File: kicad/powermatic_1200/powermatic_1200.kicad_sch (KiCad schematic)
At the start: 26 parts, among them J1 T4171310004-001, J2 3PH-4W-PLUG, K1 HMC-9B30-11-DS, K2 HMC-9B30-11-DS, K3 HC3096N-52-900-24, K4 HMC-9B30-11-DS, K5 HMC-9B30-11-DS, K6 HMC-9B30-11-DS, M1 PWRM1200-MOTOR, Q1 FAZ-D4/2-NA-L, SW1 222102

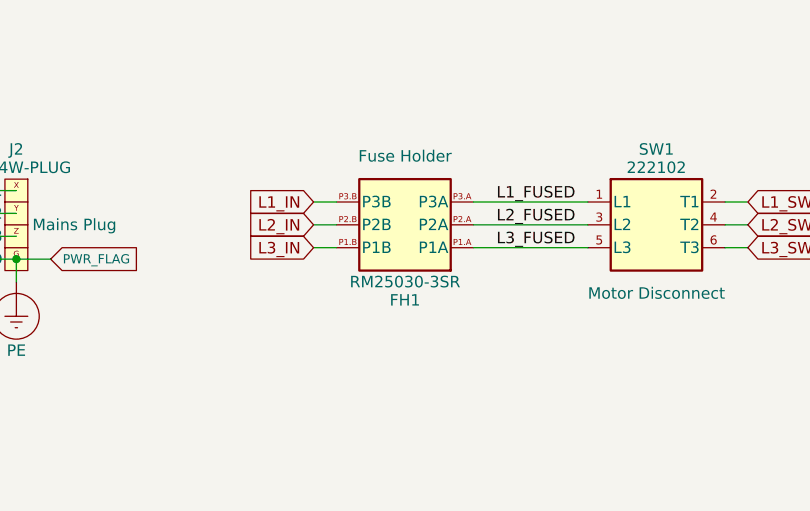
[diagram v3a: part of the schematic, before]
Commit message: Configure DIN routing grids and update fuse-holder layout
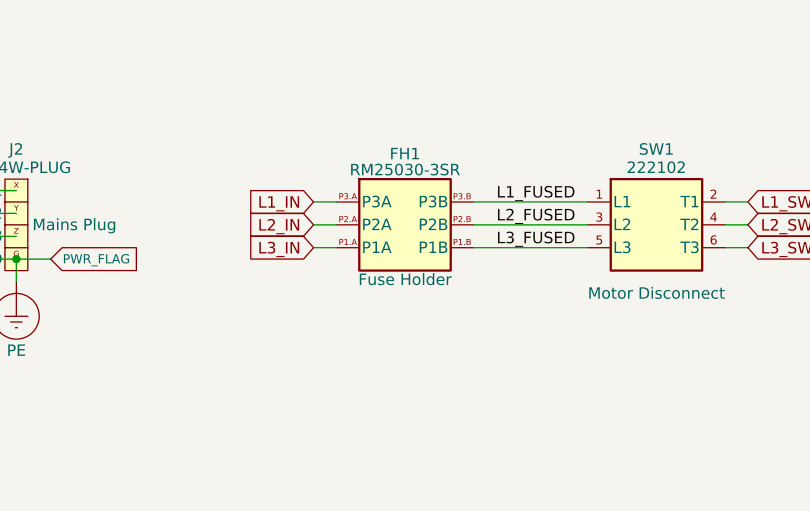
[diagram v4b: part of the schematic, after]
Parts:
- removed FH1: RM25030-3SR, Controls:RM25030-3SR_Front, symbol non_lcsc_parts:Non-LCSC/RM25030-3SR
- added FH1: RM25030-3SR, Controls:RM25030-3SR_Front, symbol Controls:RM25030-3SR
- K1, K2, K4, K5, K6: footprint Controls:HMC-9B30-11-DS_Front -> Controls:HMC-9B30-11-DS_Front_Grid1mm
- K3: footprint Controls:HC3096N-52-900-24_Front -> Controls:HC3096N-52-900-24_Front_Grid1mm
- OL4, OL6: footprint Controls:HTOR32-6-S_Front -> Controls:HTOR32-6-S_Front_Grid1mm
- PS1: footprint Controls:NDR-240-24_Front -> Controls:NDR-240-24_Front_Grid1mm
- Q1: footprint Controls:FAZ-D4-2-NA-L_Front -> Controls:FAZ-D4-2-NA-L_Front_Grid1mm
- SP1, SP2, SP4, SP5, SP6: footprint Controls:HMX1-SSVRC-DC_Front -> Controls:HMX1-SSVRC-DC_Front_Grid1mm
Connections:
- net L1_FUSED: now also FH1.P3.B (P3B)
- net L1_IN: now also FH1.P3.A (P3A)
- net L2_FUSED: now also FH1.P2.B (P2B)
- net L2_IN: now also FH1.P2.A (P2A)
- net L3_FUSED: now also FH1.P1.B (P1B)
- net L3_IN: now also FH1.P1.A (P1A)

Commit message: updated S2, S3, and M1
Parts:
- M1: footprint (none) -> Controls:PWRM1200-MOTOR_Top_150mm; Package (none) -> Machine motor (150 mm illustrative top view)
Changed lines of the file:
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@@
 		(exclude_from_sim no)
 		(in_bom yes)
-		(on_board no)
-		(in_pos_files yes)
+		(on_board yes)
+		(in_pos_files no)
 		(dnp no)
 		(property "Reference" "M1"
@@
 			)
 		)
-		(property "Footprint" ""
+		(property "Footprint" "Controls:PWRM1200-MOTOR_Top_150mm"
 			(at 302.26 -7.62 0)
 			(hide yes)
@@
 			)
 		)
-		(property "Package" ""
+		(property "Package" "Machine motor (150 mm illustrative top view)"
 			(at 302.26 -7.62 0)
 			(hide yes)

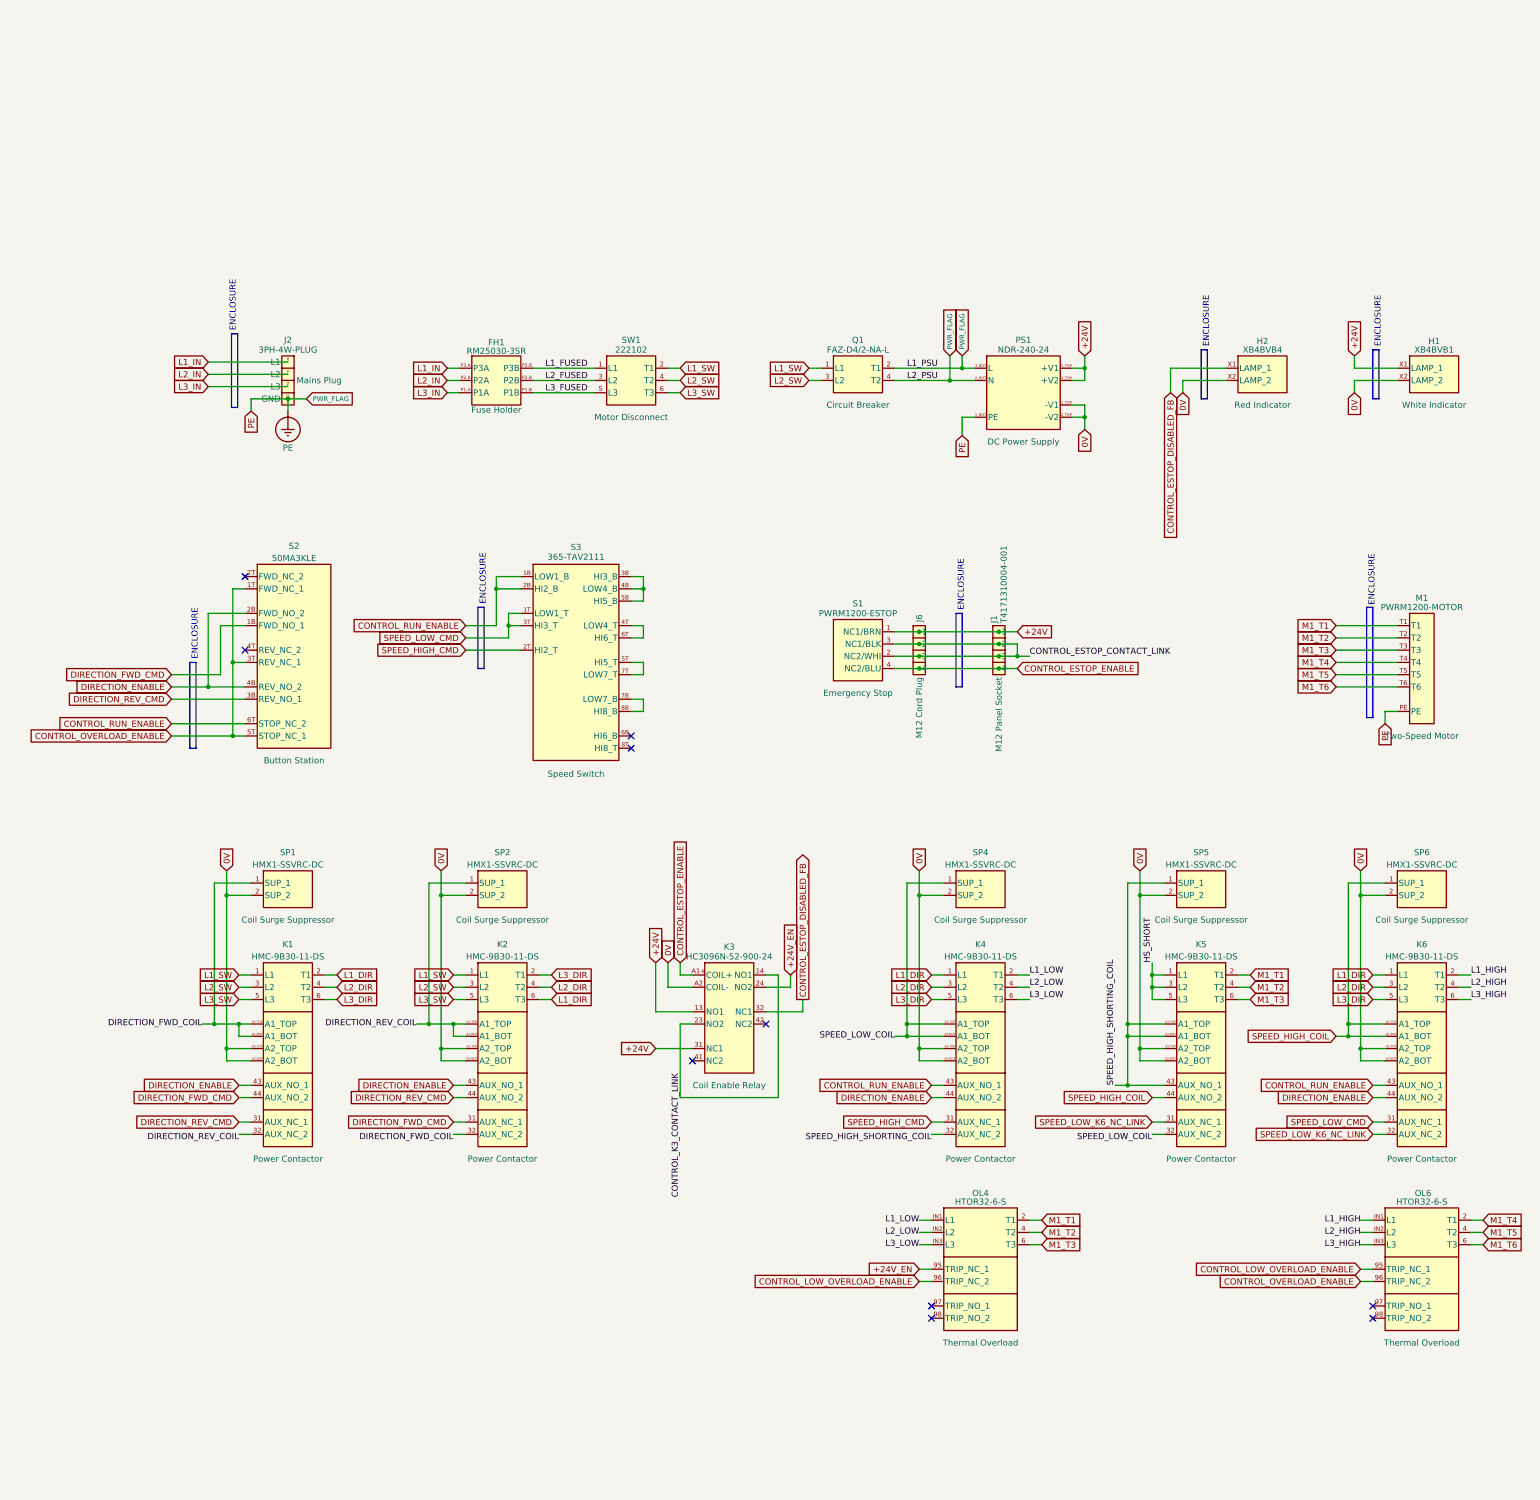
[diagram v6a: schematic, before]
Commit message: Update saved control schematic and panel layout
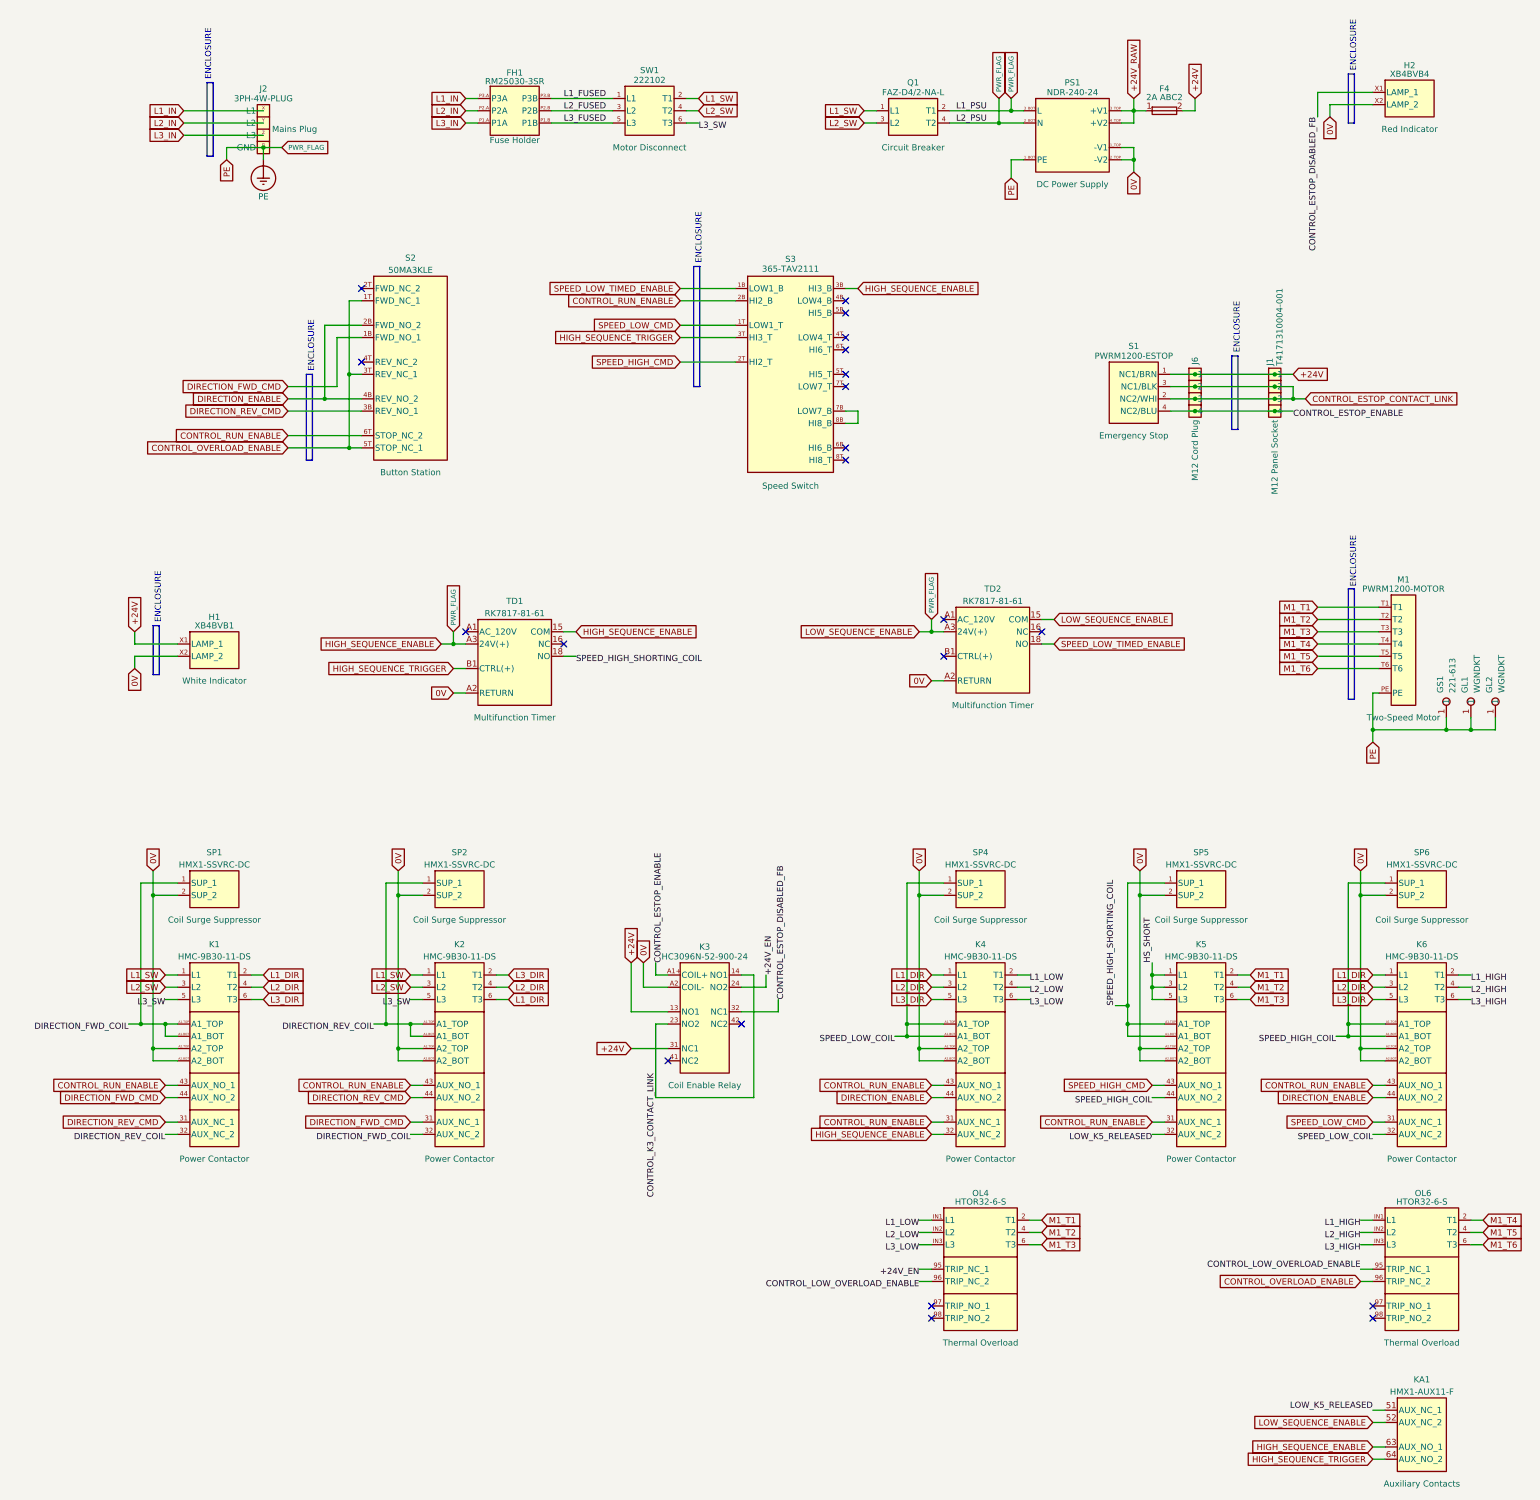
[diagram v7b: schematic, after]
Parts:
- added F4: 2A ABC2, Controls:281-623_Front, symbol Generics:Fuse
- added GL1, GL2: WGNDKT, LCSC:TestPoint_Pad_D3.0mm, symbol Generics:TestPoint
- added GS1: 221-613, LCSC:TestPoint_Pad_D3.0mm, symbol Generics:TestPoint
- added KA1: HMX1-AUX11-F, Controls:HMX1-AUX11-F_Front, symbol Controls:HMX1-AUX11-F
- added TD1, TD2: RK7817-81-61, Controls:RK7817-81-61_Front, symbol Controls:RK7817-81-61
- J1: Wire.Sizes {"schema":1,"owner_uuid":"b4d1b4ae-f9ca-4a9a-a340-a64e26a697f9","entries":[{"pin":"1","net":"+24V","scope":"factory_pigtail","awg":22,"color":"Brown","note":"T4171310004-001 factory 0.34 mm² / 22 AWG lead; any extension is a separate wire."},{"pin":"2","net":"/CONTROL_ESTOP_CONTACT_LINK","scope":"factory_pigtail","awg":22,"color":"White","note":"T4171310004-001 factory 0.34 mm² / 22 AWG lead; any extension is a separate wire."},{"pin":"3","net":"/CONTROL_ESTOP_CONTACT_LINK","scope":"factory_pigtail","awg":22,"color":"Blue","note":"T4171310004-001 factory 0.34 mm² / 22 AWG lead; any extension is a separate wire."},{"pin":"4","net":"CONTROL_ESTOP_ENABLE","scope":"factory_pigtail","awg":22,"color":"Black","note":"T4171310004-001 factory 0.34 mm² / 22 AWG lead; any extension is a separate wire."}]} -> {"schema":1,"owner_uuid":"b4d1b4ae-f9ca-4a9a-a340-a64e26a697f9","entries":[{"pin":"1","net":"+24V","scope":"factory_pigtail","awg":22,"color":"Brown","note":"T4171310004-001 factory 0.34 mm\u00b2 / 22 AWG lead; any extension is a separate wire."},{"pin":"2","net":"CONTROL_ESTOP_CONTACT_LINK","scope":"factory_pigtail","awg":22,"color":"White","note":"T4171310004-001 factory 0.34 mm\u00b2 / 22 AWG lead; any extension is a separate wire."},{"pin":"3","net":"CONTROL_ESTOP_CONTACT_LINK","scope":"factory_pigtail","awg":22,"color":"Blue","note":"T4171310004-001 factory 0.34 mm\u00b2 / 22 AWG lead; any extension is a separate wire."},{"pin":"4","net":"/CONTROL_ESTOP_ENABLE","scope":"factory_pigtail","awg":22,"color":"Black","note":"T4171310004-001 factory 0.34 mm\u00b2 / 22 AWG lead; any extension is a separate wire."}]}
- J6: Wire.Sizes {"schema":1,"owner_uuid":"b5200e46-0e22-4b8b-8db6-9eae3d708854","entries":[{"pin":"1","net":"+24V","scope":"connector_interface","awg":null,"note":"M12 mating interface; retain the supplied assembly."},{"pin":"2","net":"/CONTROL_ESTOP_CONTACT_LINK","scope":"connector_interface","awg":null,"note":"M12 mating interface; retain the supplied assembly."},{"pin":"3","net":"/CONTROL_ESTOP_CONTACT_LINK","scope":"connector_interface","awg":null,"note":"M12 mating interface; retain the supplied assembly."},{"pin":"4","net":"CONTROL_ESTOP_ENABLE","scope":"connector_interface","awg":null,"note":"M12 mating interface; retain the supplied assembly."}]} -> {"schema":1,"owner_uuid":"b5200e46-0e22-4b8b-8db6-9eae3d708854","entries":[{"pin":"1","net":"+24V","scope":"connector_interface","awg":null,"note":"M12 mating interface; retain the supplied assembly."},{"pin":"2","net":"CONTROL_ESTOP_CONTACT_LINK","scope":"connector_interface","awg":null,"note":"M12 mating interface; retain the supplied assembly."},{"pin":"3","net":"CONTROL_ESTOP_CONTACT_LINK","scope":"connector_interface","awg":null,"note":"M12 mating interface; retain the supplied assembly."},{"pin":"4","net":"/CONTROL_ESTOP_ENABLE","scope":"connector_interface","awg":null,"note":"M12 mating interface; retain the supplied assembly."}]}
- K1: footprint Controls:HMC-9B30-11-DS_Front_Grid1mm -> Controls:HMC-9B30-11-DS_Front; Wire.Sizes {"schema":1,"owner_uuid":"d223283d-de9b-4327-854a-5af43f940011","entries":[{"pin":"1","net":"L1_SW","scope":"panel_power","awg":14,"color":"Black","note":"Gauge for discrete panel wire; reversing connection-kit bars retain their supplied form."},{"pin":"2","net":"L1_DIR","scope":"panel_power","awg":14,"color":"Black","note":"Gauge for discrete panel wire; reversing connection-kit bars retain their supplied form."},{"pin":"3","net":"L2_SW","scope":"panel_power","awg":14,"color":"Black","note":"Gauge for discrete panel wire; reversing connection-kit bars retain their supplied form."},{"pin":"31","net":"DIRECTION_REV_CMD","scope":"panel_control","awg":18,"color":"Blue"},{"pin":"32","net":"/DIRECTION_REV_COIL","scope":"panel_control","awg":18,"color":"Blue"},{"pin":"4","net":"L2_DIR","scope":"panel_power","awg":14,"color":"Black","note":"Gauge for discrete panel wire; reversing connection-kit bars retain their supplied form."},{"pin":"43","net":"DIRECTION_ENABLE","scope":"panel_control","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 -> {"schema":1,"owner_uuid":"d223283d-de9b-4327-854a-5af43f940011","entries":[{"pin":"1","net":"L1_SW","scope":"panel_power","awg":14,"color":"Black","note":"Gauge for discrete panel wire; reversing connection-kit bars retain their supplied form."},{"pin":"2","net":"L1_DIR","scope":"panel_power","awg":14,"color":"Black","note":"Gauge for discrete panel wire; reversing connection-kit bars retain their supplied form."},{"pin":"3","net":"L2_SW","scope":"panel_power","awg":14,"color":"Black","note":"Gauge for discrete panel wire; reversing connection-kit bars retain their supplied form."},{"pin":"31","net":"DIRECTION_REV_CMD","scope":"panel_control","awg":18,"color":"Blue"},{"pin":"32","net":"/DIRECTION_REV_COIL","scope":"panel_control","awg":18,"color":"Blue"},{"pin":"4","net":"L2_DIR","scope":"panel_power","awg":14,"color":"Black","note":"Gauge for discrete panel wire; reversing connection-kit bars retain their supplied form."},{"pin":"43","net":"CONTROL_RUN_ENABLE","scope":"panel_control"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
- K2: footprint Controls:HMC-9B30-11-DS_Front_Grid1mm -> Controls:HMC-9B30-11-DS_Front; Wire.Sizes {"schema":1,"owner_uuid":"e654422b-9a6f-4ebb-86fa-0867c299ae4a","entries":[{"pin":"1","net":"L1_SW","scope":"panel_power","awg":14,"color":"Black","note":"Gauge for discrete panel wire; reversing connection-kit bars retain their supplied form."},{"pin":"2","net":"L3_DIR","scope":"panel_power","awg":14,"color":"Black","note":"Gauge for discrete panel wire; reversing connection-kit bars retain their supplied form."},{"pin":"3","net":"L2_SW","scope":"panel_power","awg":14,"color":"Black","note":"Gauge for discrete panel wire; reversing connection-kit bars retain their supplied form."},{"pin":"31","net":"DIRECTION_FWD_CMD","scope":"panel_control","awg":18,"color":"Blue"},{"pin":"32","net":"/DIRECTION_FWD_COIL","scope":"panel_control","awg":18,"color":"Blue"},{"pin":"4","net":"L2_DIR","scope":"panel_power","awg":14,"color":"Black","note":"Gauge for discrete panel wire; reversing connection-kit bars retain their supplied form."},{"pin":"43","net":"DIRECTION_ENABLE","scope":"panel_control","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 -> {"schema":1,"owner_uuid":"e654422b-9a6f-4ebb-86fa-0867c299ae4a","entries":[{"pin":"1","net":"L1_SW","scope":"panel_power","awg":14,"color":"Black","note":"Gauge for discrete panel wire; reversing connection-kit bars retain their supplied form."},{"pin":"2","net":"L3_DIR","scope":"panel_power","awg":14,"color":"Black","note":"Gauge for discrete panel wire; reversing connection-kit bars retain their supplied form."},{"pin":"3","net":"L2_SW","scope":"panel_power","awg":14,"color":"Black","note":"Gauge for discrete panel wire; reversing connection-kit bars retain their supplied form."},{"pin":"31","net":"DIRECTION_FWD_CMD","scope":"panel_control","awg":18,"color":"Blue"},{"pin":"32","net":"/DIRECTION_FWD_COIL","scope":"panel_control","awg":18,"color":"Blue"},{"pin":"4","net":"L2_DIR","scope":"panel_power","awg":14,"color":"Black","note":"Gauge for discrete panel wire; reversing connection-kit bars retain their supplied form."},{"pin":"43","net":"CONTROL_RUN_ENABLE","scope":"panel_control"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
- K3: footprint Controls:HC3096N-52-900-24_Front_Grid1mm -> Controls:HC3096N-52-900-24_Front; Wire.Sizes {"schema":1,"owner_uuid":"40692fa1-1db0-4fd6-bab3-8a72882b147f","entries":[{"pin":"13","net":"+24V","scope":"panel_control","awg":18,"color":"Blue"},{"pin":"14","net":"/CONTROL_K3_CONTACT_LINK","scope":"panel_control","awg":18,"color":"Blue"},{"pin":"23","net":"/CONTROL_K3_CONTACT_LINK","scope":"panel_control","awg":18,"color":"Blue"},{"pin":"24","net":"+24V_EN","scope":"panel_control","awg":18,"color":"Blue"},{"pin":"A1+","net":"CONTROL_ESTOP_ENABLE","scope":"panel_control","awg":18,"color":"Blue"},{"pin":"A2","net":"0V","scope":"panel_control","awg":18,"color":"Blue"},{"pin":"31","net":"+24V","scope":"panel_control","awg":18,"color":"Blue"},{"pin":"32","net":"CONTROL_ESTOP_DISABLED_FB","scope":"panel_control","awg":18,"color":"Blue"}]} -> {"schema":1,"owner_uuid":"40692fa1-1db0-4fd6-bab3-8a72882b147f","entries":[{"pin":"13","net":"+24V","scope":"panel_control","awg":18,"color":"Blue"},{"pin":"14","net":"/CONTROL_K3_CONTACT_LINK","scope":"panel_control","awg":18,"color":"Blue"},{"pin":"23","net":"/CONTROL_K3_CONTACT_LINK","scope":"panel_control","awg":18,"color":"Blue"},{"pin":"24","net":"/+24V_EN","scope":"panel_control","awg":18,"color":"Blue"},{"pin":"A1+","net":"/CONTROL_ESTOP_ENABLE","scope":"panel_control","awg":18,"color":"Blue"},{"pin":"A2","net":"0V","scope":"panel_control","awg":18,"color":"Blue"},{"pin":"31","net":"+24V","scope":"panel_control","awg":18,"color":"Blue"},{"pin":"32","net":"/CONTROL_ESTOP_DISABLED_FB","scope":"panel_control","awg":18,"color":"Blue"}]}
- K4: footprint Controls:HMC-9B30-11-DS_Front_Grid1mm -> Controls:HMC-9B30-11-DS_Front; Wire.Sizes {"schema":1,"owner_uuid":"e783227f-ae21-4b33-9926-7527202601c5","entries":[{"pin":"1","net":"L1_DIR","scope":"panel_power","awg":14,"color":"Black","note":"Gauge for discrete panel wire; reversing connection-kit bars retain their supplied form."},{"pin":"2","net":"/L1_LOW","scope":"direct_mount","awg":null,"note":"Direct-mounted overload power connection; no separate assembly wire."},{"pin":"3","net":"L2_DIR","scope":"panel_power","awg":14,"color":"Black","note":"Gauge for discrete panel wire; reversing connection-kit bars retain their supplied form."},{"pin":"31","net":"SPEED_HIGH_CMD","scope":"panel_control","awg":18,"color":"Blue"},{"pin":"32","net":"/SPEED_HIGH_SHORTING_COIL","scope":"panel_control","awg":18,"color":"Blue"},{"pin":"4","net":"/L2_LOW","scope":"direct_mount","awg":null,"note":"Direct-mounted overload power connection; no separate assembly wire."},{"pin":"43","net":"CONTROL_RUN_ENABLE","scope":"panel_control","awg":18,"color":"Blue"},{"pin":"44","net":"DIRECTION_ENAB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 -> {"schema":1,"owner_uuid":"e783227f-ae21-4b33-9926-7527202601c5","entries":[{"pin":"1","net":"L1_DIR","scope":"panel_power","awg":14,"color":"Black","note":"Gauge for discrete panel wire; reversing connection-kit bars retain their supplied form."},{"pin":"2","net":"/L1_LOW","scope":"direct_mount","awg":null,"note":"Direct-mounted overload power connection; no separate assembly wire."},{"pin":"3","net":"L2_DIR","scope":"panel_power","awg":14,"color":"Black","note":"Gauge for discrete panel wire; reversing connection-kit bars retain their supplied form."},{"pin":"31","net":"CONTROL_RUN_ENABLE","scope":"panel_control","awg":18,"color":"Blue"},{"pin":"32","net":"HIGH_SEQUENCE_ENABLE","scope":"panel_control","awg":18,"color":"Blue"},{"pin":"4","net":"/L2_LOW","scope":"direct_mount","awg":null,"note":"Direct-mounted overload power connection; no separate assembly wire."},{"pin":"43","net":"CONTROL_RUN_ENABLE","scope":"panel_control","awg":18,"color":"Blue"},{"pin":"44","net":"DIRECTION_ENABL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
- K5: footprint Controls:HMC-9B30-11-DS_Front_Grid1mm -> Controls:HMC-9B30-11-DS_Front; Wire.Sizes {"schema":1,"owner_uuid":"987458c8-4a51-4e1e-a1e3-3201c61e3ba1","entries":[{"pin":"1","net":"/HS_SHORT","scope":"panel_power","awg":14,"color":"Black","note":"Gauge for discrete panel wire; reversing connection-kit bars retain their supplied form."},{"pin":"2","net":"M1_T1","scope":"panel_power","awg":14,"color":"Black","note":"Gauge for discrete panel wire; reversing connection-kit bars retain their supplied form."},{"pin":"3","net":"/HS_SHORT","scope":"panel_power","awg":14,"color":"Black","note":"Gauge for discrete panel wire; reversing connection-kit bars retain their supplied form."},{"pin":"31","net":"SPEED_LOW_K6_NC_LINK","scope":"panel_control","awg":18,"color":"Blue"},{"pin":"32","net":"/SPEED_LOW_COIL","scope":"panel_control","awg":18,"color":"Blue"},{"pin":"4","net":"M1_T2","scope":"panel_power","awg":14,"color":"Black","note":"Gauge for discrete panel wire; reversing connection-kit bars retain their supplied form."},{"pin":"43","net":"/SPEED_HIGH_SHORTING_COIL","scope":"pa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 -> {"schema":1,"owner_uuid":"987458c8-4a51-4e1e-a1e3-3201c61e3ba1","entries":[{"pin":"1","net":"/HS_SHORT","scope":"panel_power","awg":14,"color":"Black","note":"Gauge for discrete panel wire; reversing connection-kit bars retain their supplied form."},{"pin":"2","net":"M1_T1","scope":"panel_power","awg":14,"color":"Black","note":"Gauge for discrete panel wire; reversing connection-kit bars retain their supplied form."},{"pin":"3","net":"/HS_SHORT","scope":"panel_power","awg":14,"color":"Black","note":"Gauge for discrete panel wire; reversing connection-kit bars retain their supplied form."},{"pin":"31","net":"CONTROL_RUN_ENABLE","scope":"panel_control","awg":18,"color":"Blue"},{"pin":"32","net":"/LOW_K5_RELEASED","scope":"panel_control","awg":18,"color":"Blue"},{"pin":"4","net":"M1_T2","scope":"panel_power","awg":14,"color":"Black","note":"Gauge for discrete panel wire; reversing connection-kit bars retain their supplied form."},{"pin":"43","net":"SPEED_HIGH_CMD","scope":"panel_control"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
- K6: footprint Controls:HMC-9B30-11-DS_Front_Grid1mm -> Controls:HMC-9B30-11-DS_Front; Wire.Sizes {"schema":1,"owner_uuid":"54a642be-21ab-409d-9820-b7dfae37b246","entries":[{"pin":"1","net":"L1_DIR","scope":"panel_power","awg":14,"color":"Black","note":"Gauge for discrete panel wire; reversing connection-kit bars retain their supplied form."},{"pin":"2","net":"/L1_HIGH","scope":"direct_mount","awg":null,"note":"Direct-mounted overload power connection; no separate assembly wire."},{"pin":"3","net":"L2_DIR","scope":"panel_power","awg":14,"color":"Black","note":"Gauge for discrete panel wire; reversing connection-kit bars retain their supplied form."},{"pin":"31","net":"SPEED_LOW_CMD","scope":"panel_control","awg":18,"color":"Blue"},{"pin":"32","net":"SPEED_LOW_K6_NC_LINK","scope":"panel_control","awg":18,"color":"Blue"},{"pin":"4","net":"/L2_HIGH","scope":"direct_mount","awg":null,"note":"Direct-mounted overload power connection; no separate assembly wire."},{"pin":"43","net":"CONTROL_RUN_ENABLE","scope":"panel_control","awg":18,"color":"Blue"},{"pin":"44","net":"DIRECTION_ENABLE",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 -> {"schema":1,"owner_uuid":"54a642be-21ab-409d-9820-b7dfae37b246","entries":[{"pin":"1","net":"L1_DIR","scope":"panel_power","awg":14,"color":"Black","note":"Gauge for discrete panel wire; reversing connection-kit bars retain their supplied form."},{"pin":"2","net":"/L1_HIGH","scope":"direct_mount","awg":null,"note":"Direct-mounted overload power connection; no separate assembly wire."},{"pin":"3","net":"L2_DIR","scope":"panel_power","awg":14,"color":"Black","note":"Gauge for discrete panel wire; reversing connection-kit bars retain their supplied form."},{"pin":"31","net":"SPEED_LOW_CMD","scope":"panel_control","awg":18,"color":"Blue"},{"pin":"32","net":"/SPEED_LOW_COIL","scope":"panel_control","awg":18,"color":"Blue"},{"pin":"4","net":"/L2_HIGH","scope":"direct_mount","awg":null,"note":"Direct-mounted overload power connection; no separate assembly wire."},{"pin":"43","net":"CONTROL_RUN_ENABLE","scope":"panel_control","awg":18,"color":"Blue"},{"pin":"44","net":"DIRECTION_ENABLE","scop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
- M1: BOM.COST (none) -> 0.00; BOM.PACK (none) -> 1; BOM.UNIT (none) -> EA; MPN (none) -> 5K_184_TFR2_7BB; Supplier (none) -> GBB; Supplier PN (none) -> 5K_184_TFR2_7BB; Wire.SizePlan {"schema":1,"owner_uuid":"f758497e-4710-4fd6-9851-f0e206557c67","entries":[{"id":"motor-body-bond","awg":10,"net":"PE","scope":"prefab_bond","from":"motor-end PE splice","to":"motor body","status":"proposed","note":"GRDKIT01 supplied assembly if selected; attachment hardware remains open."},{"id":"machine-frame-bond","awg":10,"net":"PE","scope":"prefab_bond","from":"motor-end PE splice","to":"machine frame","status":"proposed","note":"GRDKIT01 supplied assembly if selected; attachment hardware remains open."}]} -> {"schema":1,"owner_uuid":"f758497e-4710-4fd6-9851-f0e206557c67","entries":[{"id":"motor-body-bond","awg":10,"net":"PE","scope":"prefab_bond","from":"motor-box PE splice M1.PE","to":"motor bell stud J7.PE","status":"routed","note":"GRDKIT01 10 AWG factory whip; retain motor-stud ring; remove splice-end ring and strip 13 mm for WAGO 221-613.","sku":"GRDKIT01"},{"id":"machine-frame-bond","awg":10,"net":"PE","scope":"prefab_bond","from":"motor bell stud J7.PE","to":"machine frame lug J5.PE","status":"routed","note":"GRDKIT01 10 AWG factory whip; retain both factory ring lugs.","sku":"GRDKIT01"}]}; Wire.Sizes {"schema":1,"owner_uuid":"f758497e-4710-4fd6-9851-f0e206557c67","entries":[{"pin":"PE","net":"PE","scope":"motor_conduit","awg":12,"color":"Green/Yellow","note":"Motor-conduit PE to the bonding junction; attachment hardware remains installation work."},{"pin":"T1","net":"M1_T1","scope":"motor_conduit","awg":14,"color":"Black","note":"One external 14 AWG conductor per motor lead; factory motor lead size is separate."},{"pin":"T2","net":"M1_T2","scope":"motor_conduit","awg":14,"color":"Black","note":"One external 14 AWG conductor per motor lead; factory motor lead size is separate."},{"pin":"T3","net":"M1_T3","scope":"motor_conduit","awg":14,"color":"Black","note":"One external 14 AWG conductor per motor lead; factory motor lead size is separate."},{"pin":"T4","net":"M1_T4","scope":"motor_conduit","awg":14,"color":"Black","note":"One external 14 AWG conductor per motor lead; factory motor lead size is separate."},{"pin":"T5","net":"M1_T5","scope":"motor_conduit","awg":14,"color":"Black"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 -> {"schema":1,"owner_uuid":"f758497e-4710-4fd6-9851-f0e206557c67","entries":[{"pin":"PE","net":"PE","scope":"connector_interface","color":"Green/Yellow","note":"WAGO 221-613 common PE splice. Separate ports receive 12 AWG conduit PE and 10 AWG GRDKIT01 bonds; the other wire endpoint assigns its gauge."},{"pin":"T1","net":"M1_T1","scope":"motor_conduit","awg":14,"color":"Black","note":"One external 14 AWG conductor per motor lead; factory motor lead size is separate."},{"pin":"T2","net":"M1_T2","scope":"motor_conduit","awg":14,"color":"Black","note":"One external 14 AWG conductor per motor lead; factory motor lead size is separate."},{"pin":"T3","net":"M1_T3","scope":"motor_conduit","awg":14,"color":"Black","note":"One external 14 AWG conductor per motor lead; factory motor lead size is separate."},{"pin":"T4","net":"M1_T4","scope":"motor_conduit","awg":14,"color":"Black","note":"One external 14 AWG conductor per motor lead; factory motor lead size is separate."},{"pin":"T5","net":"M1_T5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
- OL4: footprint Controls:HTOR32-6-S_Front_Grid1mm -> Controls:HTOR32-6-S_Front; Wire.Sizes {"schema":1,"owner_uuid":"8f9cbdae-7fda-4d4b-8774-5d7141934ea9","entries":[{"pin":"2","net":"M1_T1","scope":"panel_power","awg":14,"color":"Black"},{"pin":"4","net":"M1_T2","scope":"panel_power","awg":14,"color":"Black"},{"pin":"6","net":"M1_T3","scope":"panel_power","awg":14,"color":"Black"},{"pin":"95","net":"+24V_EN","scope":"panel_control","awg":18,"color":"Blue"},{"pin":"96","net":"CONTROL_LOW_OVERLOAD_ENABLE","scope":"panel_control","awg":18,"color":"Blue"},{"pin":"IN1","net":"/L1_LOW","scope":"direct_mount","awg":null,"note":"Direct-mounted overload power connection; no separate assembly wire."},{"pin":"IN2","net":"/L2_LOW","scope":"direct_mount","awg":null,"note":"Direct-mounted overload power connection; no separate assembly wire."},{"pin":"IN3","net":"/L3_LOW","scope":"direct_mount","awg":null,"note":"Direct-mounted overload power connection; no separate assembly wire."}]} -> {"schema":1,"owner_uuid":"8f9cbdae-7fda-4d4b-8774-5d7141934ea9","entries":[{"pin":"2","net":"M1_T1","scope":"panel_power","awg":14,"color":"Black"},{"pin":"4","net":"M1_T2","scope":"panel_power","awg":14,"color":"Black"},{"pin":"6","net":"M1_T3","scope":"panel_power","awg":14,"color":"Black"},{"pin":"95","net":"/+24V_EN","scope":"panel_control","awg":18,"color":"Blue"},{"pin":"96","net":"/CONTROL_LOW_OVERLOAD_ENABLE","scope":"panel_control","awg":18,"color":"Blue"},{"pin":"IN1","net":"/L1_LOW","scope":"direct_mount","awg":null,"note":"Direct-mounted overload power connection; no separate assembly wire."},{"pin":"IN2","net":"/L2_LOW","scope":"direct_mount","awg":null,"note":"Direct-mounted overload power connection; no separate assembly wire."},{"pin":"IN3","net":"/L3_LOW","scope":"direct_mount","awg":null,"note":"Direct-mounted overload power connection; no separate assembly wire."}]}
- OL6: footprint Controls:HTOR32-6-S_Front_Grid1mm -> Controls:HTOR32-6-S_Front; Wire.Sizes {"schema":1,"owner_uuid":"bcd2f5c5-5bd2-4363-a1dd-539e3135e608","entries":[{"pin":"2","net":"M1_T4","scope":"panel_power","awg":14,"color":"Black"},{"pin":"4","net":"M1_T5","scope":"panel_power","awg":14,"color":"Black"},{"pin":"6","net":"M1_T6","scope":"panel_power","awg":14,"color":"Black"},{"pin":"95","net":"CONTROL_LOW_OVERLOAD_ENABLE","scope":"panel_control","awg":18,"color":"Blue"},{"pin":"96","net":"CONTROL_OVERLOAD_ENABLE","scope":"panel_control","awg":18,"color":"Blue"},{"pin":"IN1","net":"/L1_HIGH","scope":"direct_mount","awg":null,"note":"Direct-mounted overload power connection; no separate assembly wire."},{"pin":"IN2","net":"/L2_HIGH","scope":"direct_mount","awg":null,"note":"Direct-mounted overload power connection; no separate assembly wire."},{"pin":"IN3","net":"/L3_HIGH","scope":"direct_mount","awg":null,"note":"Direct-mounted overload power connection; no separate assembly wire."}]} -> {"schema":1,"owner_uuid":"bcd2f5c5-5bd2-4363-a1dd-539e3135e608","entries":[{"pin":"2","net":"M1_T4","scope":"panel_power","awg":14,"color":"Black"},{"pin":"4","net":"M1_T5","scope":"panel_power","awg":14,"color":"Black"},{"pin":"6","net":"M1_T6","scope":"panel_power","awg":14,"color":"Black"},{"pin":"95","net":"/CONTROL_LOW_OVERLOAD_ENABLE","scope":"panel_control","awg":18,"color":"Blue"},{"pin":"96","net":"CONTROL_OVERLOAD_ENABLE","scope":"panel_control","awg":18,"color":"Blue"},{"pin":"IN1","net":"/L1_HIGH","scope":"direct_mount","awg":null,"note":"Direct-mounted overload power connection; no separate assembly wire."},{"pin":"IN2","net":"/L2_HIGH","scope":"direct_mount","awg":null,"note":"Direct-mounted overload power connection; no separate assembly wire."},{"pin":"IN3","net":"/L3_HIGH","scope":"direct_mount","awg":null,"note":"Direct-mounted overload power connection; no separate assembly wire."}]}
- PS1: footprint Controls:NDR-240-24_Front_Grid1mm -> Controls:NDR-240-24_Front; Wire.Sizes {"schema":1,"owner_uuid":"b71e1787-97a1-40f8-b061-785c348498c6","entries":[{"pin":"1_BOT","net":"PE","scope":"panel_pe","awg":14,"color":"Green/Yellow"},{"pin":"1_TOP","net":"0V","scope":"panel_control","awg":18,"color":"Blue","note":"PSU duplicate output terminals are internally common; no jumper is implied."},{"pin":"2_BOT","net":"/L2_PSU","scope":"panel_power","awg":14,"color":"Black"},{"pin":"2_TOP","net":"0V","scope":"panel_control","awg":18,"color":"Blue","note":"PSU duplicate output terminals are internally common; no jumper is implied."},{"pin":"3_BOT","net":"/L1_PSU","scope":"panel_power","awg":14,"color":"Black"},{"pin":"3_TOP","net":"+24V","scope":"panel_control","awg":18,"color":"Blue","note":"PSU duplicate output terminals are internally common; no jumper is implied."},{"pin":"4_TOP","net":"+24V","scope":"panel_control","awg":18,"color":"Blue","note":"PSU duplicate output terminals are internally common; no jumper is implied."}]} -> {"schema":1,"owner_uuid":"b71e1787-97a1-40f8-b061-785c348498c6","entries":[{"pin":"1_BOT","net":"PE","scope":"panel_pe","awg":14,"color":"Green/Yellow"},{"pin":"1_TOP","net":"0V","scope":"panel_control","awg":18,"color":"Blue","note":"PSU duplicate output terminals are internally common; no jumper is implied."},{"pin":"2_BOT","net":"/L2_PSU","scope":"panel_power","awg":14,"color":"Black"},{"pin":"2_TOP","net":"0V","scope":"panel_control","awg":18,"color":"Blue","note":"PSU duplicate output terminals are internally common; no jumper is implied."},{"pin":"3_BOT","net":"/L1_PSU","scope":"panel_power","awg":14,"color":"Black"},{"pin":"3_TOP","net":"+24V_RAW","scope":"panel_control","awg":18,"color":"Blue","note":"PSU duplicate output terminals are internally common; no jumper is implied."},{"pin":"4_TOP","net":"+24V_RAW","scope":"panel_control","awg":18,"color":"Blue","note":"PSU duplicate output terminals are internally common; no jumper is implied."}]}
- Q1: footprint Controls:FAZ-D4-2-NA-L_Front_Grid1mm -> Controls:FAZ-D4-2-NA-L_Front
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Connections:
- net +24V: now also F4.2; no longer PS1.3_TOP (+V1), PS1.4_TOP (+V2)
- net 0V: now also TD1.A2 (RETURN), TD2.A2 (RETURN)
- net CONTROL_RUN_ENABLE: now also K1.43 (AUX_NO_1), K2.43 (AUX_NO_1), K4.31 (AUX_NC_1), K5.31 (AUX_NC_1); no longer S3.1B (LOW1_B)
- net DIRECTION_ENABLE: no longer K1.43 (AUX_NO_1), K2.43 (AUX_NO_1)
- net PE: now also GL1.1, GL2.1, GS1.1
- net SPEED_HIGH_CMD: now also K5.43 (AUX_NO_1); no longer K4.31 (AUX_NC_1)
- net SPEED_HIGH_SHORTING_COIL: now also TD1.18 (NO); no longer K4.32 (AUX_NC_2), K5.43 (AUX_NO_1)
- net SPEED_LOW_CMD: no longer S3.3T (HI3_T)
- net SPEED_LOW_COIL: now also K6.32 (AUX_NC_2); no longer K5.32 (AUX_NC_2)
- net at S3.4T (LOW4_T): no longer S3.6T (HI6_T)
- net at S3.5T (HI5_T): no longer S3.7T (LOW7_T)
- removed net SPEED_LOW_K6_NC_LINK: K5.31 (AUX_NC_1), K6.32 (AUX_NC_2)
- new net +24V_RAW: F4.1, PS1.3_TOP (+V1), PS1.4_TOP (+V2)
- new net HIGH_SEQUENCE_ENABLE: K4.32 (AUX_NC_2), KA1.63 (AUX_NO_1), S3.3B (HI3_B), TD1.15 (COM), TD1.A3 (24V(+))
- new net HIGH_SEQUENCE_TRIGGER: KA1.64 (AUX_NO_2), S3.3T (HI3_T), TD1.B1 (CTRL(+))
- new net LOW_K5_RELEASED: K5.32 (AUX_NC_2), KA1.51 (AUX_NC_1)
- new net LOW_SEQUENCE_ENABLE: KA1.52 (AUX_NC_2), TD2.15 (COM), TD2.A3 (24V(+))
- new net SPEED_LOW_TIMED_ENABLE: S3.1B (LOW1_B), TD2.18 (NO)
- now unconnected: S3.4B (LOW4_B), S3.5B (HI5_B)
- no-connect marks 10 -> 21
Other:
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
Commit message: Use supplied door bond and separate J-box grounding branches
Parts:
- M1: Wire.SizePlan {"schema":1,"owner_uuid":"f758497e-4710-4fd6-9851-f0e206557c67","entries":[{"id":"motor-body-bond","awg":10,"net":"PE","scope":"prefab_bond","from":"motor-box PE splice M1.PE","to":"motor bell stud J7.PE","status":"routed","note":"GRDKIT01 10 AWG factory whip; retain motor-stud ring; remove splice-end ring and strip 13 mm for WAGO 221-613.","sku":"GRDKIT01"},{"id":"machine-frame-bond","awg":10,"net":"PE","scope":"prefab_bond","from":"motor bell stud J7.PE","to":"machine frame lug J5.PE","status":"routed","note":"GRDKIT01 10 AWG factory whip; retain both factory ring lugs.","sku":"GRDKIT01"}]} -> {"schema":1,"owner_uuid":"f758497e-4710-4fd6-9851-f0e206557c67","entries":[{"id":"motor-body-bond","awg":10,"net":"PE","scope":"prefab_bond","from":"motor-box PE splice M1.PE","to":"motor bell stud J7.PE","status":"routed","note":"GRDKIT01 10 AWG factory whip; retain motor-stud ring; remove splice-end ring and strip 13 mm for WAGO 221-613.","sku":"GRDKIT01"},{"id":"machine-frame-bond","awg":10,"net":"PE","scope":"prefab_bond","from":"motor-box PE splice M1.PE","to":"machine frame lug J5.PE","status":"routed","note":"GRDKIT01 10 AWG factory whip directly from J-box WAGO 221-613 to frame; retain frame ring, remove splice-end ring and strip 13 mm.","sku":"GRDKIT01"}]}
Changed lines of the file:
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@@
 			)
 		)
-		(property "Wire.SizePlan" "{\"schema\":1,\"owner_uuid\":\"f758497e-4710-4fd6-9851-f0e206557c67\",\"entries\":[{\"id\":\"motor-body-bond\",\"awg\":10,\"net\":\"PE\",\"scope\":\"prefab_bond\",\"from\":\"motor-box PE splice M1.PE\",\"to\":\"motor bell stud J7.PE\",\"status\":\"routed\",\"note\":\"GRDKIT01 10 AWG factory whip; retain motor-stud ring; remove splice-end ring and strip 13 mm for WAGO 221-613.\",\"sku\":\"GRDKIT01\"},{\"id\":\"machine-frame-bond\",\"awg\":10,\"net\":\"PE\",\"scope\":\"prefab_bond\",\"from\":\"motor bell stud J7.PE\",\"to\":\"machine frame lug J5.PE\",\"status\":\"routed\",\"note\":\"GRDKIT01 10 AWG factory whip; retain both factory ring lugs.\",\"sku\":\"GRDKIT01\"}]}"
+		(property "Wire.SizePlan" "{\"schema\":1,\"owner_uuid\":\"f758497e-4710-4fd6-9851-f0e206557c67\",\"entries\":[{\"id\":\"motor-body-bond\",\"awg\":10,\"net\":\"PE\",\"scope\":\"prefab_bond\",\"from\":\"motor-box PE splice M1.PE\",\"to\":\"motor bell stud J7.PE\",\"status\":\"routed\",\"note\":\"GRDKIT01 10 AWG factory whip; retain motor-stud ring; remove splice-end ring and strip 13 mm for WAGO 221-613.\",\"sku\":\"GRDKIT01\"},{\"id\":\"machine-frame-bond\",\"awg\":10,\"net\":\"PE\",\"scope\":\"prefab_bond\",\"from\":\"motor-box PE splice M1.PE\",\"to\":\"machine frame lug J5.PE\",\"status\":\"routed\",\"note\":\"GRDKIT01 10 AWG factory whip directly from J-box WAGO 221-613 to frame; retain frame ring, remove splice-end ring and strip 13 mm.\",\"sku\":\"GRDKIT01\"}]}"
 			(at 298.45 -11.43 0)
 			(hide yes)
